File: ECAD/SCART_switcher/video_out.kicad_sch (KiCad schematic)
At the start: 36 parts, among them Q30 BC857, U63 AD8054, U64 74LVC1G04, U65 AD8054

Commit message: Progressed ECAD.
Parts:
- renumbered C69 to C100, C70 to C101, C71 to C102, C72 to C103, C73 to C104, C74 to C105, C75 to C106, C76 to C107, C77 to C108, C78 to C109, C66 to C97, C67 to C98, C68 to C99, U63 to U74, U64 to U75, U65 to U76

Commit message: Progressed ECAD.
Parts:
- C100, C102, C107, C109: footprint Capacitor_SMD:C_0805_2012Metric -> Capacitor_SMD:C_1206_3216Metric; MPN CL21B104KBCNNNC -> GRM31C5C1H104JA01L; Status (none) -> OK
- C103, C104, C97: footprint Capacitor_SMD:C_0805_2012Metric -> Capacitor_SMD:C_0603_1608Metric

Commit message: Progressed ECAD.
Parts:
- removed U75: 74LVC1G04, Package_TO_SOT_SMD:SOT-353_SC-70-5, symbol 74xGxx:74AHC1G04
- added D25: BAS16W, Package_TO_SOT_SMD:SOT-323_SC-70, symbol Diode:BAS16W
- added R119: 4k7R, Resistor_SMD:R_0805_2012Metric, symbol Device:R
- added U74: LMV331, symbol Comparator:LMV331
- renumbered C101 to C100, C102 to C101, C103 to C102, C104 to C103, C105 to C104, C106 to C105, C107 to C106, C108 to C107, C109 to C108, C97 to C96, C98 to C97, C99 to C98, C100 to C99, Q30 to Q29, U74 to U73, U76 to U75
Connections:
- net +5V: now also R119.1, U74.5 (V+)
- net BLANKING_IN: now also U74.3 (-)
- net GND: now also D25.3 (K), U74.2 (V-)
- net at R126.1: now also U74.4
- new net 0.7V: D25.1 (A), R119.2, U74.1 (+)
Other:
- moved on the sheet: C102, Q29, R126, R127, R128

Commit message: Progressed ECAD.
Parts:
- added R124: 10kR, Resistor_SMD:R_0805_2012Metric, symbol Device:R
- U74: footprint (none) -> Package_TO_SOT_SMD:SOT-23-5; MPN (none) -> LMV331IDBVR; Status (none) -> OK
- renumbered R124 to R125, R125 to R126, R126 to R127, R127 to R128, R128 to R129, R129 to R130, R130 to R131, R131 to R132, R132 to R133, R133 to R134, R134 to R135, R135 to R136, R136 to R137, R137 to R138, R138 to R139
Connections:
- net +5V: now also R124.1
- net 0.7V: now also U74.3 (-); no longer U74.1 (+)
- net BLANKING_IN: now also U74.1 (+); no longer U74.3 (-)
- net at R127.1, U74.4: now also R124.2
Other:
- note removed: "BLANKING output stage"
- moved on the sheet: U74

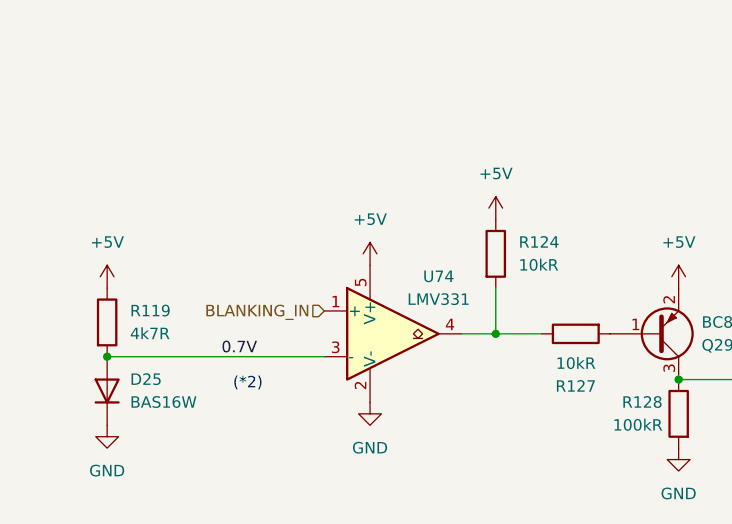
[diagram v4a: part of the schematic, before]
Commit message: Update video_out.kicad_sch
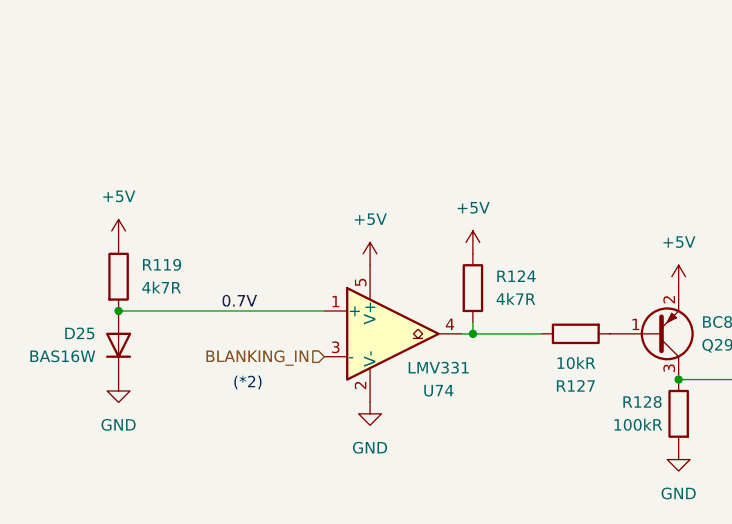
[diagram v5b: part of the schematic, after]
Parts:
- R124: value 10kR -> 4k7R; MPN RC0805FR-0710KL -> (none)
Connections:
- net 0.7V: now also U74.1 (+); no longer U74.3 (-)
- net BLANKING_IN: now also U74.3 (-); no longer U74.1 (+)
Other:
- moved on the sheet: D25, R119

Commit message: Progressed ECAD.
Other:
- note added: "I=120mA"
- note added: "I=1mA"
- note added: "I=40mA"
- note added: "I_{on}=0.1mA"
- note added: "I_{on}=1mA"
- note added: "I_{on}=30mA"
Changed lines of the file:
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@@
+    (effects (font (size 1.27 1.27)) (justify left bottom))
+  )
+  (text "I_{on}=30mA" (at 99.06 154.94 0)
     (effects (font (size 1.27 1.27)) (justify left bottom))
   )
@@
     (effects (font (size 1.27 1.27)) (justify left bottom))
   )
+  (text "I=1mA" (at 38.1 149.86 0)
+    (effects (font (size 1.27 1.27)) (justify left bottom))
+  )
+  (text "I=40mA" (at 62.23 100.33 0)
+    (effects (font (size 1.27 1.27)) (justify left bottom))
+  )
   (text "(*2) BLANKING pin has the following signaling:\n	Level 0: 0 V to 0.4 V (Composite video mode)\n	Level 1: +1 V to +3 V (RGB video mode)"
     (at 177.8 176.53 0)
     (effects (font (size 1.27 1.27)) (justify left bottom))
   )
+  (text "I_{on}=1mA" (at 76.2 151.13 0)
+    (effects (font (size 1.27 1.27)) (justify left bottom))
+  )
+  (text "I_{on}=0.1mA" (at 64.77 152.4 0)
+    (effects (font (size 1.27 1.27)) (justify left bottom))
+  )
+  (text "I=120mA" (at 184.15 100.33 0)
+    (effects (font (size 1.27 1.27)) (justify left bottom))
+  )

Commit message: Progressed ECAD.
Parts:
- renumbered C96 to C100, C97 to C101, C98 to C102, C99 to C103, C100 to C104, C101 to C105, C102 to C106, C103 to C107, C104 to C108, C105 to C109, C106 to C110, C107 to C111, C108 to C112, R119 to R121, R120 to R122, R121 to R123, R122 to R124, R123 to R125, R124 to R126, R125 to R127, R126 to R128, R127 to R129, R128 to R130, R129 to R131, R130 to R132, R131 to R133, R132 to R134, R133 to R135, R134 to R136, R135 to R137, R136 to R138, R137 to R139, R138 to R140, R139 to R141, U73 to U74, U74 to U75, U75 to U76

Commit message: Progressed ECAD.
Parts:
- renumbered C102 to C100, C103 to C101, C104 to C102, C105 to C103, C106 to C104, C107 to C105, C108 to C106, C109 to C107, C110 to C108, C111 to C109, C112 to C110, C100 to C98, C101 to C99, R121 to R119, R122 to R120, R123 to R121, R124 to R122, R125 to R123, R126 to R124, R127 to R125, R128 to R126, R129 to R127, R130 to R128, R131 to R129, R132 to R130, R133 to R131, R134 to R132, R135 to R133, R136 to R134, R137 to R135, R138 to R136, R139 to R137, R140 to R138, R141 to R139
